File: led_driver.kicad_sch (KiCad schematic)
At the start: 32 parts, among them J1 BarrelJack_3167288, J2 USB4105-GF-A, U1 MP2483DQ-LF-P, U2 AP62301Z6-7

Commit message: Finalized board layout
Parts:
- removed C6: C_10p_0402, antmicro-footprints:C_0402_1005Metric, symbol antmicroCapacitors0402:C_10p_0402
- added C13: C_100n_0402, antmicro-footprints:C_0402_1005Metric, symbol antmicroCapacitors0402:C_100n_0402
- added C6: C_10u_25V_0603, antmicro-footprints:C_0603_1608Metric, symbol antmicroCapacitors0603:C_10u_25V_0603
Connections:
- net +12V: now also C6.2
- net GND: now also C13.1, C6.1
- net VBUS: now also C13.2
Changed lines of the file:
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@@
     (stroke (width 0) (type default) (color 0 0 0 0))
   )
-  (wire (pts (xy 383.54 142.875) (xy 388.62 142.875))
+  (wire (pts (xy 383.54 142.875) (xy 394.335 142.875))
     (stroke (width 0) (type default) (color 0 0 0 0))
   )
@@
     (stroke (width 0) (type default) (color 0 0 0 0))
   )
+  (wire (pts (xy 394.335 153.035) (xy 394.335 158.115))
+    (stroke (width 0) (type default) (color 0 0 0 0))
+  )
   (wire (pts (xy 238.125 77.47) (xy 238.125 67.945))
     (stroke (width 0) (type default) (color 0 0 0 0))
@@
   )
   (wire (pts (xy 71.755 67.31) (xy 76.835 67.31))
+    (stroke (width 0) (type default) (color 0 0 0 0))
+  )
+  (wire (pts (xy 394.335 147.955) (xy 394.335 142.875))
     (stroke (width 0) (type default) (color 0 0 0 0))
   )
@@
     )
     (property "Datasheet" "" (id 3) (at 204.47 160.655 0)
+      (effects (font (size 1.27 1.27)) hide)
+    )
+    (pin "1")
+  )
+  (symbol (lib_id "power:GND") (at 394.335 158.115 0) (unit 1)
+    (in_bom yes) (on_board yes) (fields_autoplaced)
+    (property "Reference" "#PWR015" (id 0) (at 394.335 164.465 0)
+      (effects (font (size 1.27 1.27)) hide)
+    )
+    (property "Value" "GND" (id 1) (at 394.335 163.195 0))
+    (property "Footprint" "" (id 2) (at 394.335 158.115 0)
+      (effects (font (size 1.27 1.27)) hide)
+    )
+    (property "Datasheet" "" (id 3) (at 394.335 158.115 0)
       (effects (font (size 1.27 1.27)) hide)
     )
@@
     (pin "EPAD")
   )
+  (symbol (lib_id "antmicroCapacitors0402:C_100n_0402") (at 394.335 153.035 90) (unit 1)
+    (in_bom yes) (on_board yes) (fields_autoplaced)
+    (property "Reference" "C13" (id 0) (at 396.875 149.2185 90)
+      (effects (font (size 1.27 1.27) (thickness 0.15)) (justify right))
+    )
+    (property "Value" "C_100n_0402" (id 1) (at 404.495 132.715 0)
+      (effects (font (size 1.27 1.27) (thickness 0.15)) (justify left bottom) hide)
+    )
+    (property "Footprint" "antmicro-footprints:C_0402_1005Metric" (id 2) (at 407.035 132.715 0)
+      (effects (font (size 1.27 1.27) (thickness 0.15)) (justify left bottom) hide)
+    )
+    (property "Datasheet" "https://search.murata.co.jp/Ceramy/image/img/A01X/G101/ENG/GRM155R61H104KE14-01.pdf" (id 3) (at 409.575 132.715 0)
+      (effects (font (size 1.27 1.27) (thickness 0.15)) (justify left bottom) hide)
+    )
+    (property "MPN" "GRM155R61H104KE14D" (id 4) (at 412.115 132.715 0)
+      (effects (font (size 1.27 1.27) (thickness 0.15)) (justify left bottom) hide)
+    )
+    (property "Manufacturer" "Murata" (id 5) (at 414.655 132.715 0)
+      (effects (font (size 1.27 1.27) (thickness 0.15)) (justify left bottom) hide)
+    )
+    (property "License" "Apache-2.0 License" (id 6) (at 417.195 132.715 0)
+      (effects (font (size 1.27 1.27) (thickness 0.15)) (justify left bottom) hide)
+    )
+    (property "Copyright" "Copyright (c) 2023 Antmicro" (id 7) (at 419.735 132.715 0)
+      (effects (font (size 1.27 1.27) (thickness 0.15)) (justify left bottom) hide)
+    )
+    (property "Val" "100n" (id 8) (at 396.875 151.7585 90)
+      (effects (font (size 1.27 1.27) (thickness 0.15)) (justify right))
+    )
+    (property "Voltage" "50V" (id 9) (at 422.275 132.715 0)
+      (effects (font (size 1.27 1.27)) (justify left bottom) hide)
+    )
+    (property "Dielectric" "X5R" (id 10) (at 424.815 132.715 0)
+      (effects (font (size 1.27 1.27)) (justify left bottom) hide)
+    )
+    (pin "1")
+    (pin "2")
+  )
   (symbol (lib_id "antmicroResistors0402:R_1k3_0402") (at 227.33 76.2 90) (unit 1)
     (in_bom yes) (on_board yes) (fields_autoplaced)
@@
     (pin "1")
   )
+  (symbol (lib_id "antmicroCapacitors0603:C_10u_25V_0603") (at 163.195 66.04 90) (unit 1)
+    (in_bom yes) (on_board yes) (fields_autoplaced)
+    (property "Reference" "C6" (id 0) (at 166.37 62.2235 90)
+      (effects (font (size 1.27 1.27) (thickness 0.15)) (justify right))
+    )
+    (property "Value" "C_10u_25V_0603" (id 1) (at 173.355 45.72 0)
+      (effects (font (size 1.27 1.27) (thickness 0.15)) (justify left bottom) hide)
+    )
+    (property "Footprint" "antmicro-footprints:C_0603_1608Metric" (id 2) (at 175.895 45.72 0)
+      (effects (font (size 1.27 1.27) (thickness 0.15)) (justify left bottom) hide)
+    )
+    (property "Datasheet" "template_datasheet" (id 3) (at 178.435 45.72 0)
+      (effects (font (size 1.27 1.27) (thickness 0.15)) (justify left bottom) hide)
+    )
+    (property "MPN" "C1608X5R1E106M080AC" (id 4) (at 180.975 45.72 0)
+      (effects (font (size 1.27 1.27) (thickness 0.15)) (justify left bottom) hide)
+    )
+    (property "Manufacturer" "TDK" (id 5) (at 183.515 45.72 0)
+      (effects (font (size 1.27 1.27) (thickness 0.15)) (justify left bottom) hide)
+    )
+    (property "License" "Apache-2.0 License" (id 6) (at 186.055 45.72 0)
+      (effects (font (size 1.27 1.27) (thickness 0.15)) (justify left bottom) hide)
+    )
+    (property "Copyright" "Copyright (c) 2023 Antmicro" (id 7) (at 188.595 45.72 0)
+      (effects (font (size 1.27 1.27) (thickness 0.15)) (justify left bottom) hide)
+    )
+    (property "Val" "10u/25V" (id 8) (at 166.37 64.7635 90)
+      (effects (font (size 1.27 1.27) (thickness 0.15)) (justify right))
+    )
+    (property "Voltage" "" (id 9) (at 191.135 45.72 0)
+      (effects (font (size 1.27 1.27)) (justify left bottom) hide)
+    )
+    (property "Dielectric" "" (id 10) (at 193.675 45.72 0)
+      (effects (font (size 1.27 1.27)) (justify left bottom) hide)
+    )
+    (pin "1")
+    (pin "2")
+  )
   (symbol (lib_id "antmicroResistors0402:R_6k8_0402") (at 227.33 64.77 90) (unit 1)
     (in_bom yes) (on_board yes) (fields_autoplaced)
@@
       (effects (font (size 1.27 1.27)) (justify left bottom) hide)
     )
-    (pin "1")
-    (pin "2")
-  )
-  (symbol (lib_id "antmicroCapacitors0402:C_10p_0402") (at 163.195 60.96 270) (unit 1)
-    (in_bom yes) (on_board yes) (fields_autoplaced)
-    (property "Reference" "C6" (id 0) (at 165.735 62.2362 90)
-      (effects (font (size 1.27 1.27) (thickness 0.15)) (justify left))
-    )
-    (property "Value" "C_10p_0402" (id 1) (at 153.035 81.28 0)
-      (effects (font (size 1.27 1.27) (thickness 0.15)) (justify left bottom) hide)
-    )
-    (property "Footprint" "antmicro-footprints:C_0402_1005Metric" (id 2) (at 150.495 81.28 0)
-      (effects (font (size 1.27 1.27) (thickness 0.15)) (justify left bottom) hide)
-    )
-    (property "Datasheet" "https://search.murata.co.jp/Ceramy/image/img/A01X/G101/ENG/GCM1555C1H100GA16-01.pdf" (id 3) (at 147.955 81.28 0)
-      (effects (font (size 1.27 1.27) (thickness 0.15)) (justify left bottom) hide)
-    )
-    (property "MPN" "GCM1555C1H100GA16D" (id 4) (at 145.415 81.28 0)
-      (effects (font (size 1.27 1.27) (thickness 0.15)) (justify left bottom) hide)
-    )
-    (property "Manufacturer" "Murata" (id 5) (at 142.875 81.28 0)
-      (effects (font (size 1.27 1.27) (thickness 0.15)) (justify left bottom) hide)
-    )
-    (property "License" "Apache-2.0 License" (id 6) (at 140.335 81.28 0)
-      (effects (font (size 1.27 1.27) (thickness 0.15)) (justify left bottom) hide)
-    )
-    (property "Copyright" "Copyright (c) 2023 Antmicro" (id 7) (at 137.795 81.28 0)
-      (effects (font (size 1.27 1.27) (thickness 0.15)) (justify left bottom) hide)
-    )
-    (property "Val" "10p" (id 8) (at 165.735 64.7762 90)
-      (effects (font (size 1.27 1.27) (thickness 0.15)) (justify left))
-    )
-    (property "Voltage" "50V" (id 9) (at 135.255 81.28 0)
-      (effects (font (size 1.27 1.27)) (justify left bottom) hide)
-    )
-    (property "Dielectric" "C0G" (id 10) (at 132.715 81.28 0)
-      (effects (font (size 1.27 1.27)) (justify left bottom) hide)
-    )

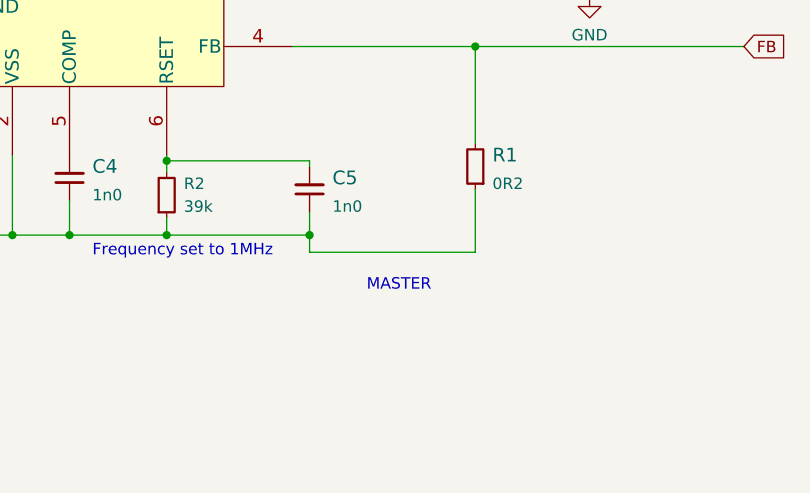
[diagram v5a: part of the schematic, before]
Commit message: Power rail routing changes
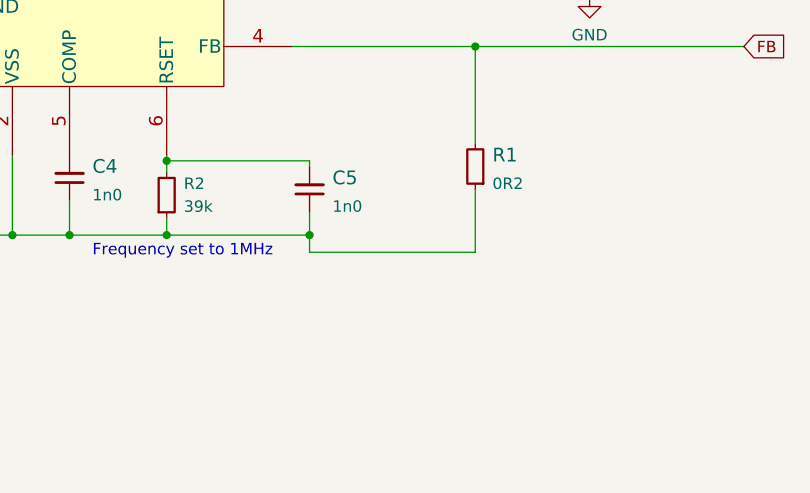
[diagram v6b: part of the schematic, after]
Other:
- note removed: "MASTER"
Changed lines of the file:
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@@
     (effects (font (size 3 3)) (justify left bottom))
-  )
-  (text "MASTER\n" (at 167.005 232.41 0)
-    (effects (font (size 1.27 1.27)) (justify left bottom))
   )
   (text "USB C output" (at 332.105 111.76 0)

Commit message: Update naming convention
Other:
- title: (none) -> LZ1 OSRAM LuxiGen LED Driver
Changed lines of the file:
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@@
 (kicad_sch (version 20211123) (generator eeschema)
   (paper "A3")
+  (title_block
+    (title "LZ1 OSRAM LuxiGen LED Driver")
+    (date "2023-05-04")
+    (rev "1.0.0")
+    (comment 1 "www.antmicro.com")
+  )
   (junction (at 127.635 226.06) (diameter 0) (color 0 0 0 0)
   )
